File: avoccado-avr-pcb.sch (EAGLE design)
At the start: 30 parts, among them IC1 MCP1703CB, IC5 ATMEGA328P-20MU, Q1 #MHz, Q2 MOSFET-NCHANNEL2N7002PW, U1 ATMEGA328P, U2 MCP73831, X1 Micro USB

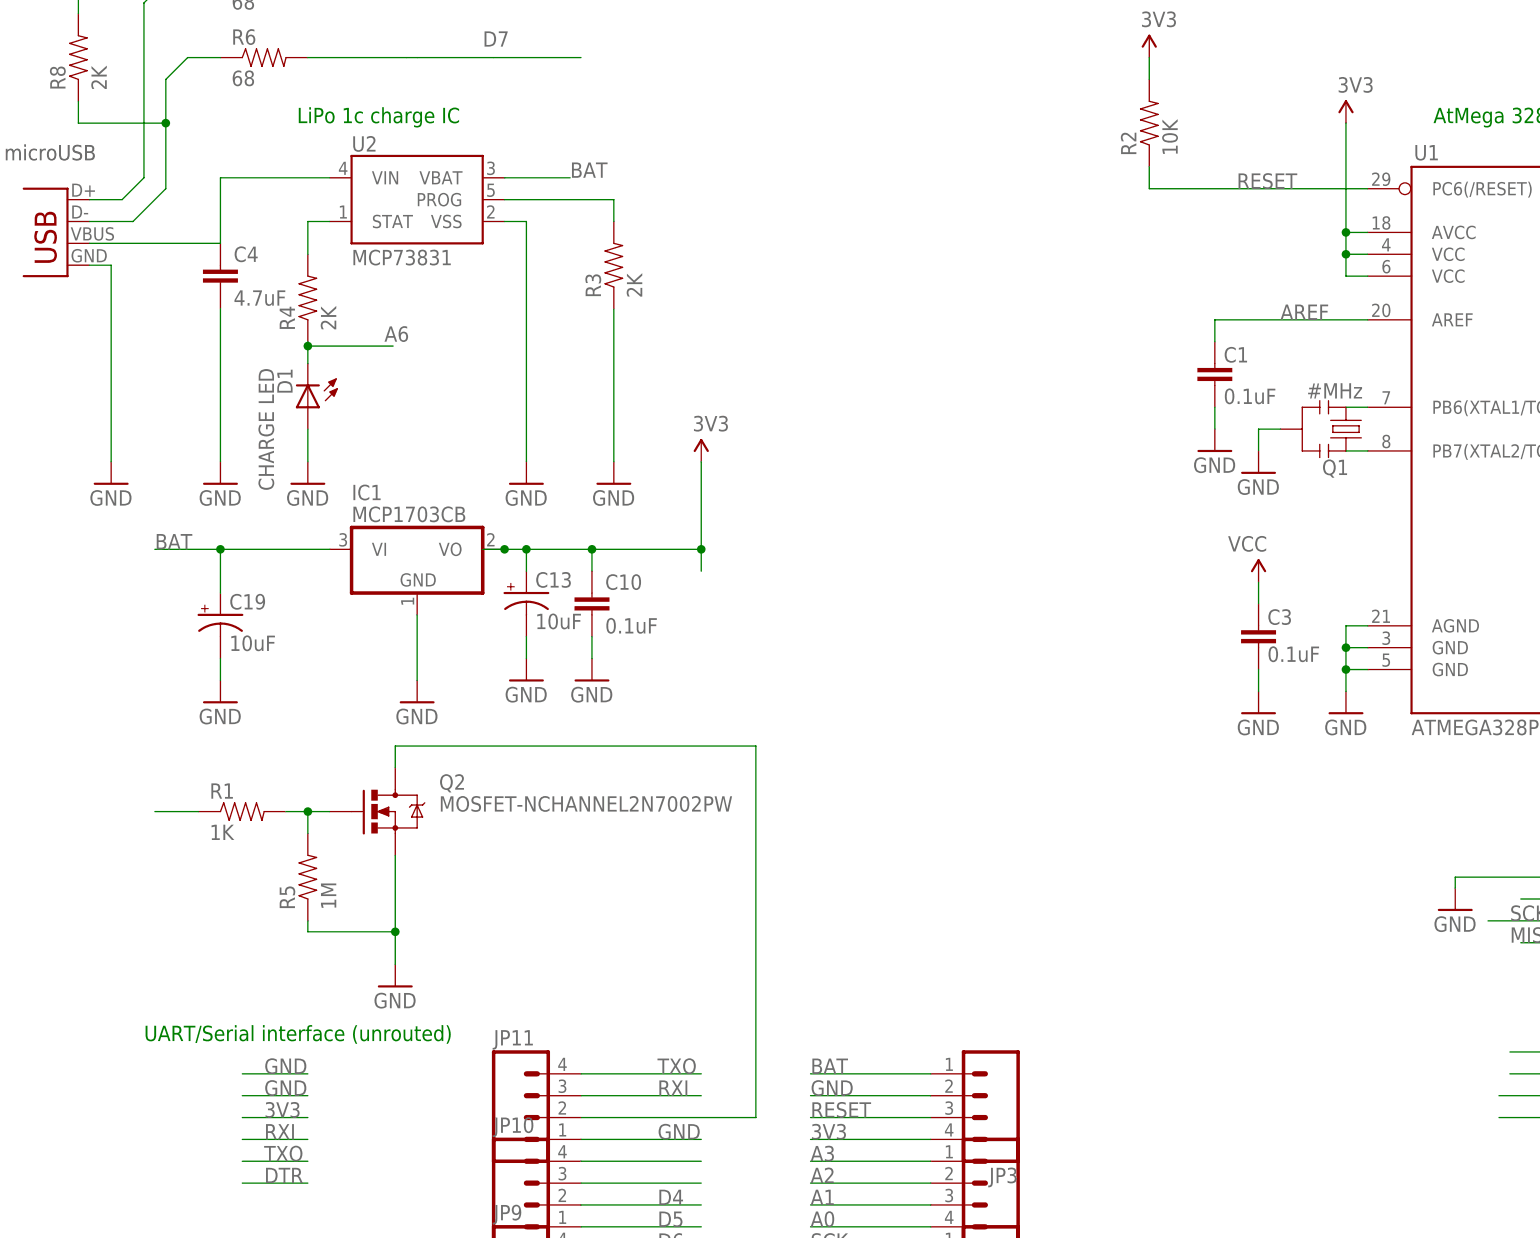
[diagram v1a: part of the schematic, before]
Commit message: increase board size to 19x42
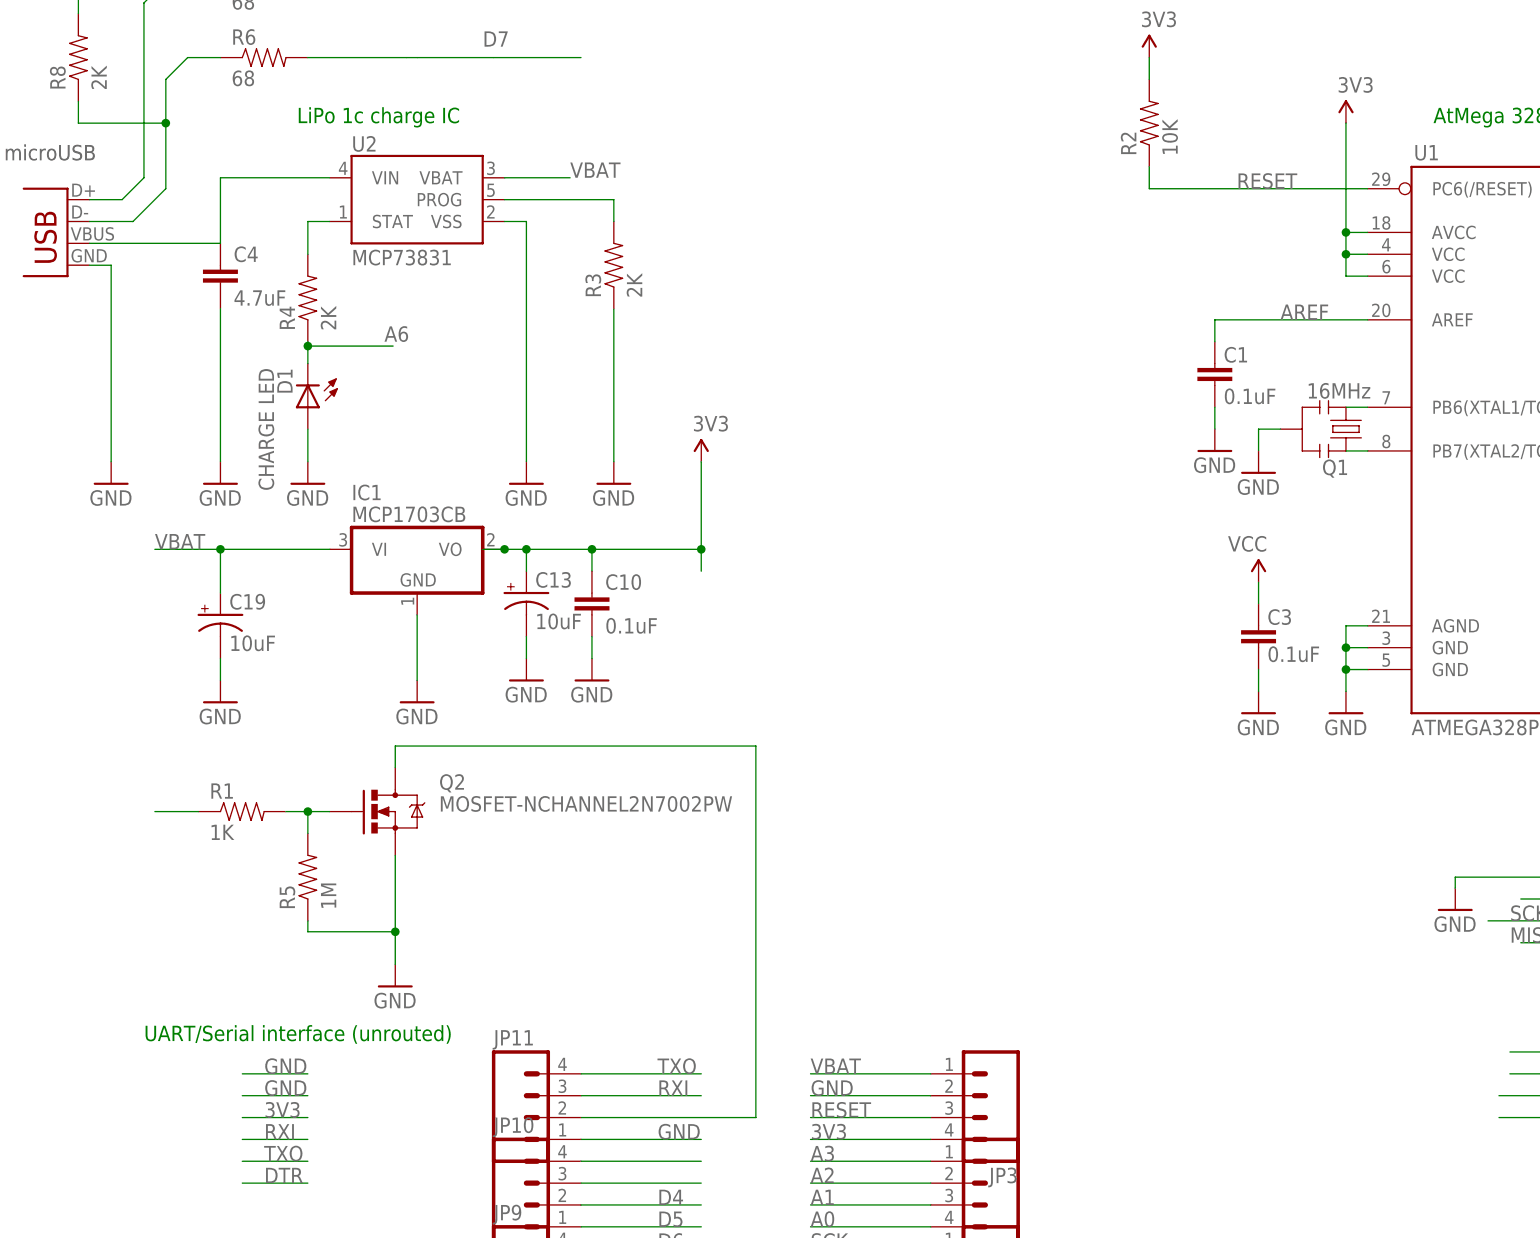
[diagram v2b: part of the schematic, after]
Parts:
- Q1: value #MHz -> 16MHz
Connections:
- net BAT renamed VBAT
- removed net N$9: IC5.PD1(TXD)
- net TXO: now also IC5.PD1(TXD)
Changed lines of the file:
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@@
 <part name="P+12" library="SparkFun" deviceset="3.3V" device="" value="3V3"/>
 <part name="P+15" library="SparkFun" deviceset="3.3V" device="" value="VCC"/>
-<part name="Q1" library="SparkFun" deviceset="RESONATOR" device="SMD" value="#MHz"/>
+<part name="Q1" library="SparkFun" deviceset="RESONATOR" device="SMD" value="16MHz"/>
 <part name="GND4" library="SparkFun" deviceset="GND" device=""/>
 <part name="U1" library="SparkFun-DigitalIC" deviceset="ATMEGA328_SMT" device="" value="ATMEGA328P"/>
@@
 <label x="39.37" y="41.91" size="1.778" layer="95"/>
 </segment>
+<segment>
+<pinref part="IC5" gate="G$1" pin="PD1(TXD)"/>
+<wire x1="215.9" y1="200.66" x2="228.6" y2="200.66" width="0.1524" layer="91"/>
+</segment>
 </net>
 <net name="3V3" class="0">
@@
 </segment>
 </net>
-<net name="BAT" class="1">
+<net name="VBAT" class="1">
 <segment>
 <pinref part="U2" gate="G$1" pin="VBAT"/>
@@
 </segment>
 </net>
-<net name="N$9" class="0">
-<segment>
-<pinref part="IC5" gate="G$1" pin="PD1(TXD)"/>
-<wire x1="215.9" y1="200.66" x2="228.6" y2="200.66" width="0.1524" layer="91"/>
-</segment>
-</net>

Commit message: change MPU6050 locked header to straight one
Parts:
- JP1: device SparkFun-Connectors:M04LOCK -> SparkFun-Connectors:M041X04_NO_SILK
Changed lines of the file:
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@@
 <part name="R6" library="SparkFun-Resistors" deviceset="RESISTOR" device="0603" value="68"/>
 <part name="R7" library="SparkFun-Resistors" deviceset="RESISTOR" device="0603" value="68"/>
-<part name="JP1" library="SparkFun-Connectors" deviceset="M04" device="LOCK"/>
+<part name="JP1" library="SparkFun-Connectors" deviceset="M04" device="1X04_NO_SILK"/>
 <part name="IC5" library="idii" deviceset="MEGA8" device="-MI" value="ATMEGA328P-20MU"/>
 <part name="GND16" library="SparkFun" deviceset="GND" device=""/>
@@
 </segment>
 <segment>
-<wire x1="182.88" y1="49.53" x2="199.39" y2="49.53" width="0.1524" layer="91"/>
 <pinref part="JP1" gate="G$1" pin="3"/>
 <label x="193.294" y="49.53" size="1.778" layer="95"/>
+<wire x1="182.88" y1="49.53" x2="199.39" y2="49.53" width="0.1524" layer="91"/>
 </segment>
 <segment>
@@
 </segment>
 <segment>
-<wire x1="182.88" y1="46.99" x2="199.39" y2="46.99" width="0.1524" layer="91"/>
 <pinref part="JP1" gate="G$1" pin="4"/>
 <label x="193.294" y="46.99" size="1.778" layer="95"/>
-</segment>
-<segment>
+<wire x1="182.88" y1="46.99" x2="199.39" y2="46.99" width="0.1524" layer="91"/>
+</segment>
+<segment>

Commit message: silkscreen placed
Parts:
- D1: value CHARGE LED -> LED
- Q2: value MOSFET-NCHANNEL2N7002PW -> FET
- renumbered IC1 to LDO, JP1 to MPU6050, U1 to AVR
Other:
- note removed: "Released under the Creative Commons Attribution Share-Alike 4.0 License"
